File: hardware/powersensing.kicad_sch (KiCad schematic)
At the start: 4 parts, among them U3 INA228

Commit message: poweroutput: AP74502Q kullanıcı çıkış anahtarını ekle (REV_C 3.4, 3.2 #3)
Kullanıcı akımı artık Q3/Q4'ten geçmiyor; şöntün arkasındaki dallanma
noktasından (PD_VBUS_SENSED) M1/M2 back-to-back FET çifti üzerinden akıyor.
Yol kaybı yarıya iniyor.

Bileşenler (14): U12 AP74502Q, Q5/Q6 back-to-back NMOS (60V 4mR TBD),
D6 BZT52C12 GATE-SRC zener, D7 SMBJ30A çıkış TVS, R54 1k + C30 22nF
soft-start, R55/R56 232k/10k OVLO, R57/R58 10k/100k EN ağı, R59 10k bleed,
C31 220nF VCAP, C32 100nF VIN.

OVLO bölücü hesabı: V(OVR) = 1.25 V tip -> 232k/10k = 30.25 V tipik,
tolerans uçlarında 28.2-32.3 V. Bölücü akımı 124 uA, OV kaçağı 110 nA max.

3.2 #3: powersensing'deki PD_VOUT etiketi SW_OUT oldu. INA228 Vin+ ve
RShunt1 artık M2 drain'inden besleniyor, PD_VOUT'tan değil.

Doğrulama (netlist)
- PD_VBUS_SENSED: Q5.3 ve R55.1 eklendi (şönt sonrası dallanma)
- GATE_DRV: U12.6, Q5.1, Q6.1, D6.1, R54.1
- SRC_COMMON: U12.8, Q5.2, Q6.2, D6.2
- SW_OUT: Q6.3, RShunt1.1, U3.10  |  OUT_POS: RShunt1.2, U3.8, U3.9, J4.1, D7.1, R59.1
- INA_ALERT wired-OR: U12.1, U3.3, U2.26, R57.2, R58.1
- PD_VOUT artık RShunt1 ve U3.10 içermiyor

AÇIK: OUT_EN hiçbir yere bağlı değil (ERC isolated_pin_label uyarısı).
ESP32-C6-WROOM-1'in 29 pininin tamamı kullanımda, boş GPIO yok. Doküman
3.5 yeni bir strapping olmayan GPIO istiyor ama pin bütçesi buna uygun
değil. GPIO seçimi firmware ve pin haritasını etkilediği için atanmadı.

Sayfa A4 -> A3.

Co-Authored-By: Claude Opus 5 <noreply@anthropic.com>
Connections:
- net PD_VOUT renamed SW_OUT
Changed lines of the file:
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@@
 		)
 	)
-	(global_label "PD_VOUT"
+	(global_label "SW_OUT"
 		(shape passive)
 		(at 71.12 118.11 180)

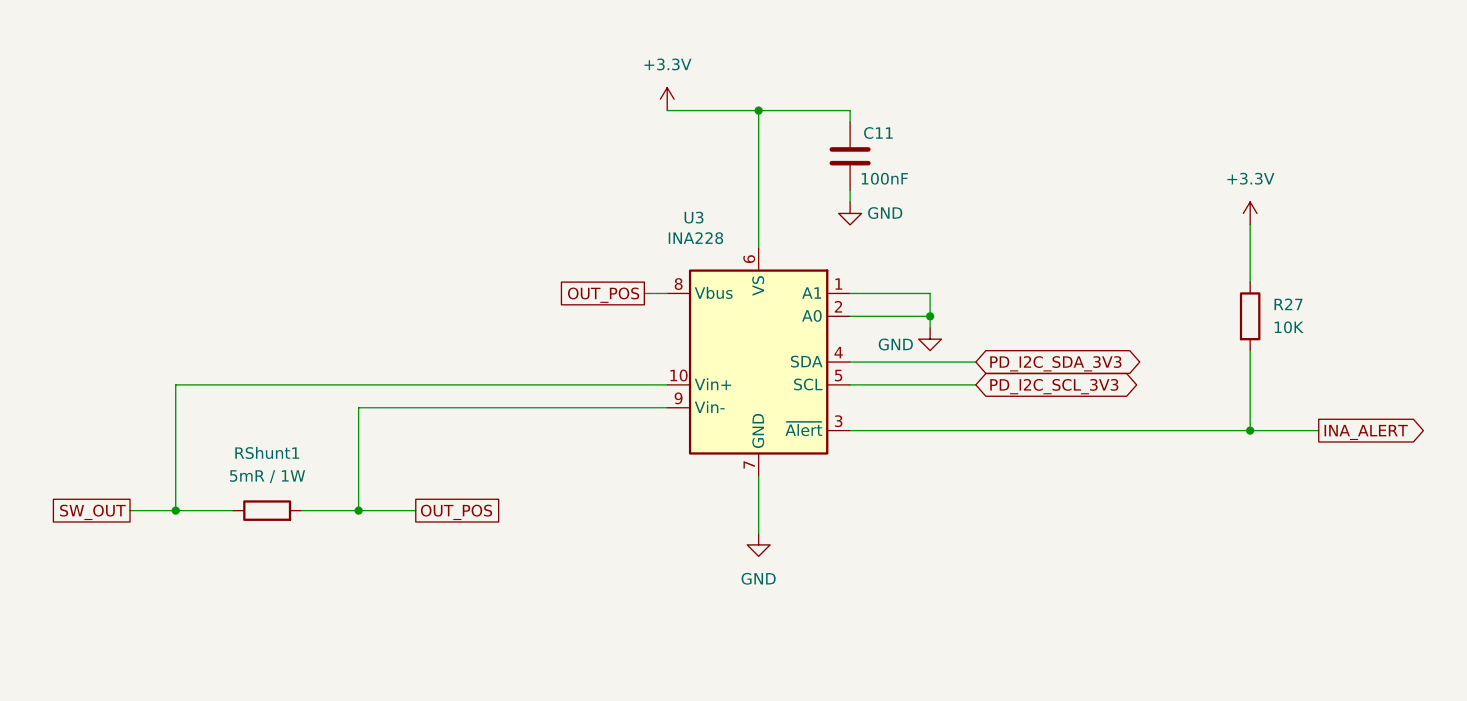
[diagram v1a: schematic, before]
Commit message: usb_pd_controller, mcu, powersensing: çizimleri yeniden düzenle, SDA dönüştürücüsünü bağla
Çizim (netlist aşağıdaki düzeltme dışında aynı)
- usb_pd_controller: üç blok (AP33772S kontrolcü, VBUS şönt + çıkış
  anahtarı, I2C seviye dönüştürücü). Q3/Q4 kapıları tek tel hattıyla,
  Q3 ang 90 + mirror y. TestPoint değer yazıları gizli.
- mcu: ESP32, RTC ve test noktası blokları. Sağ kenar satırları kesişmesiz;
  GPIO8 strap ağı satır sonunda, GPIO9 BOOT ağı dıştan aşağı. EN RC + RESET
  IC'nin üstüne alındı. UART/I2C/INT test noktaları etiketle ayrı blokta.
- powersensing: INA228 bloğu, şönt Kelvin bağlantısı kesişmesiz.

Devre düzeltmesi (kullanıcı onaylı)
- SDA seviye dönüştürücüsü kopuktu: R6.2 ve Q2.D bağlı değildi,
  PD_I2C_SDA_5V etiketi boştaydı. SCL tarafıyla (R5/Q1) simetrik bağlandı.
- Netlist farkı: PD_I2C_SDA_5V += Q2.3, R6.2;
  unconnected-(Q2-D-Pad3) ve unconnected-(R6-Pad2) kalktı.
- ERC 5 -> 2 (0 hata). Kalanlar: TL431DBZ lib_symbol_mismatch, OUT_EN
  isolated_pin_label (GPIO seçimi bekliyor).

Co-Authored-By: Claude Opus 5 <noreply@anthropic.com>
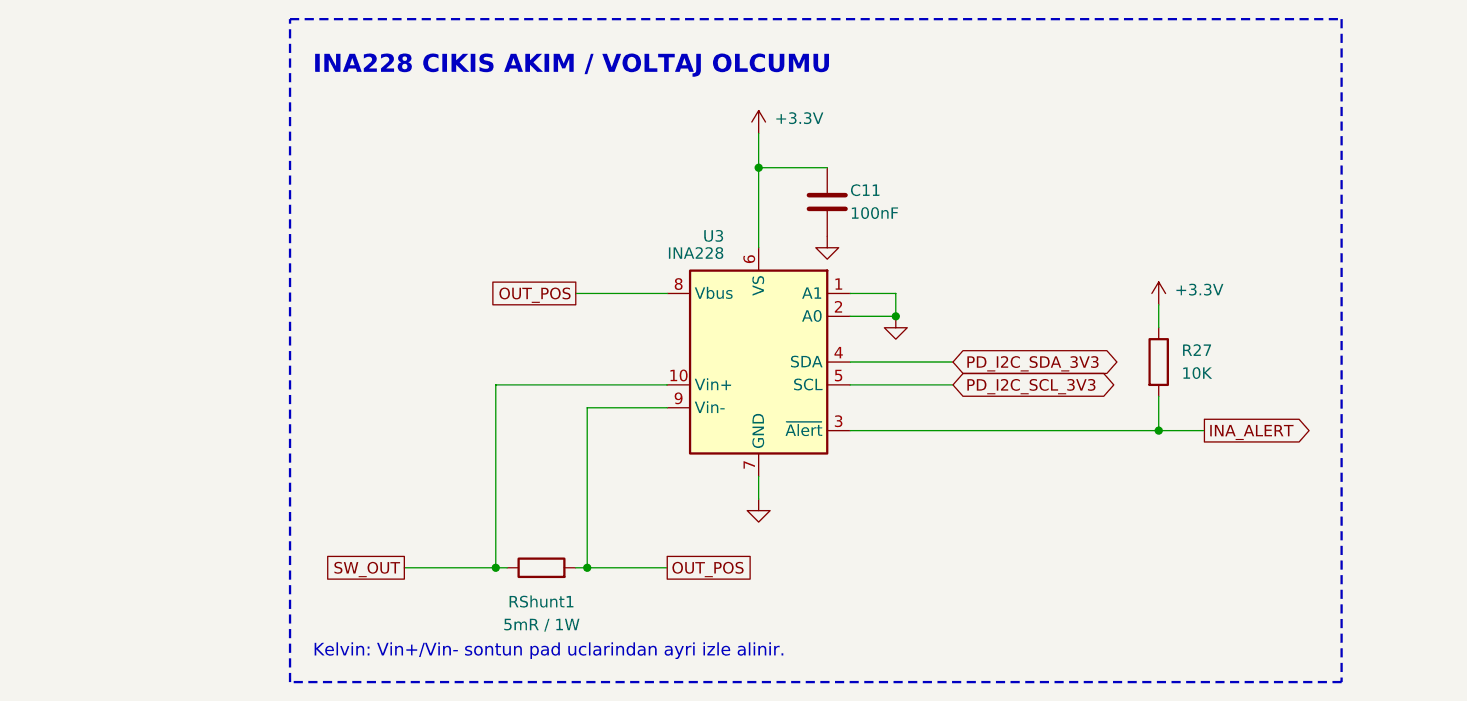
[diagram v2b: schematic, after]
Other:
- note added: "INA228 CIKIS AKIM / VOLTAJ OLCUMU"
- note added: "Kelvin: Vin+/Vin- sontun pad uclarindan ayri izle alinir."
- moved on the sheet: C11, R27, RShunt1
